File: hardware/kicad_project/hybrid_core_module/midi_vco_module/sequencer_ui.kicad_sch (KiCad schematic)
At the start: 53 parts, among them SW10 RotaryEncoder, SW6 SW_Push, SW7 SW_Push, SW8 SW_Push, SW9 SW_SP3T_NR01103, U25 MCP23017_SO

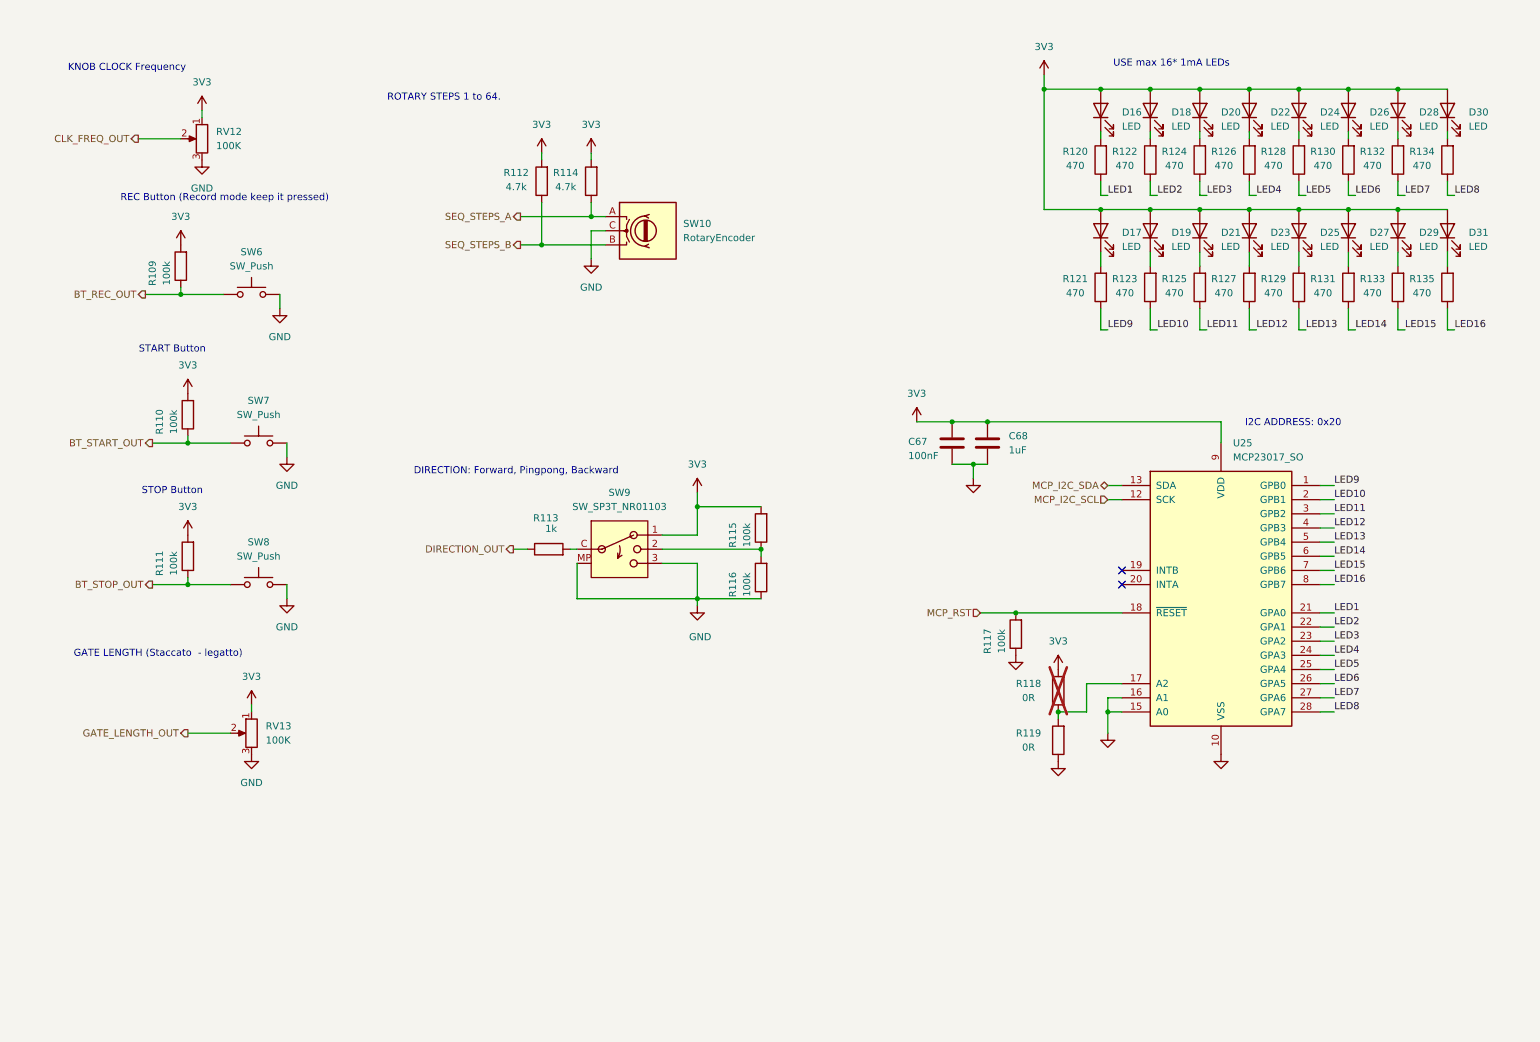
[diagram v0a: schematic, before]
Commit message: Schematic updated. Components Footprint assignment started. Waiting for components mechanical validation before starting layout.
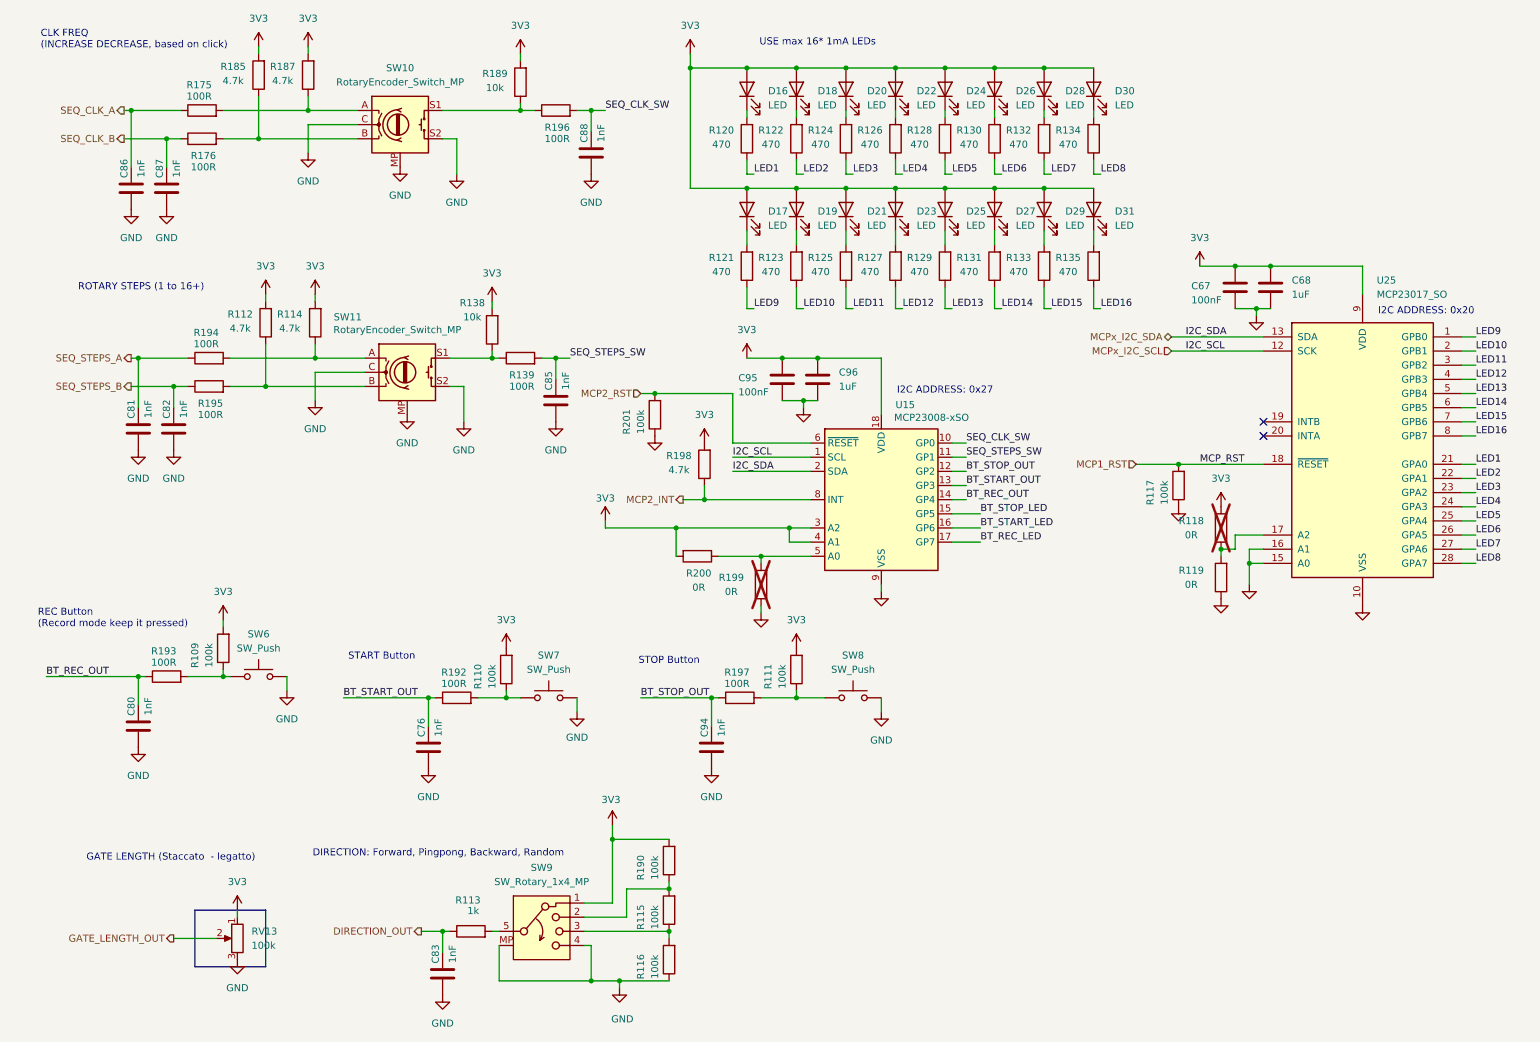
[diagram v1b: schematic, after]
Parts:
- removed RV12: 100K, symbol Device:R_Potentiometer
- removed SW10: RotaryEncoder, symbol Device:RotaryEncoder
- removed SW9: SW_SP3T_NR01103, Button_Switch_THT:SW_NKK_NR01, symbol Switch:SW_SP3T_NR01103
- added C76, C80, C81, C82, C83, C85, C86, C87, C88, C94: 1nF, Capacitor_SMD:C_0402_1005Metric, symbol Device:C
- added C95: 100nF, Capacitor_SMD:C_0402_1005Metric, symbol Device:C
- added C96: 1uF, Capacitor_SMD:C_0805_2012Metric, symbol Device:C
- added R138, R189: 10k, Resistor_SMD:R_0402_1005Metric, symbol Device:R
- added R139, R175, R176, R192, R193, R194, R195, R196, R197: 100R, Resistor_SMD:R_0402_1005Metric, symbol Device:R
- added R185, R187, R198: 4.7k, Resistor_SMD:R_0402_1005Metric, symbol Device:R
- added R190, R201: 100k, Resistor_SMD:R_0402_1005Metric, symbol Device:R
- added R199, R200: 0R, Resistor_SMD:R_0402_1005Metric, symbol Device:R
- added SW10, SW11: RotaryEncoder_Switch_MP, symbol Device:RotaryEncoder_Switch_MP
- added SW9: SW_Rotary_1x4_MP, symbol Switch:SW_Rotary_1x4_MP
- added U15: MCP23008-xSO, Package_SO:SOIC-18W_7.5x11.6mm_P1.27mm, symbol Interface_Expansion:MCP23008-xSO
- C67: footprint (none) -> Capacitor_SMD:C_0402_1005Metric; Manufacturer (none) -> MURATA; Manufacturer PartNumer (none) -> GRM155R71E104KE14J
- C68: footprint (none) -> Capacitor_SMD:C_0805_2012Metric; Manufacturer (none) -> MURATA; Manufacturer PartNumer (none) -> GRM219R71E105MA88J
- D17, D18, D19, D20, D21, D22, D23, D24, D25, D26, D27, D28, D29, D30, D31: footprint (none) -> mylib:LED-3528
- R109, R110, R111, R115, R116, R117: footprint (none) -> Resistor_SMD:R_0402_1005Metric; Manufacturer (none) -> YAGEO; Manufacturer PartNumer (none) -> RT0402FRE07100KL
- R112, R114: footprint (none) -> Resistor_SMD:R_0402_1005Metric; Manufacturer (none) -> YAGEO; Manufacturer PartNumer (none) -> RT0402FRE074K7L
- R113: footprint (none) -> Resistor_SMD:R_0402_1005Metric; Manufacturer (none) -> YAGEO; Manufacturer PartNumer (none) -> RT0402FRE071KL
- R118, R119: footprint (none) -> Resistor_SMD:R_0402_1005Metric; Manufacturer (none) -> YAGEO; Manufacturer PartNumer (none) -> RC0402FR-070RL
- R120, R121, R122, R123, R124, R125, R126, R127, R128, R129, R130, R131, R132, R133, R134, R135: footprint (none) -> Resistor_SMD:R_0402_1005Metric; Manufacturer (none) -> YAGEO; Manufacturer PartNumer (none) -> RT0402FRE07470RL
- RV13: value 100K -> 100k
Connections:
- net 3V3: now also C95.1, C96.1, R138.2, R185.2, R187.2, R189.2, R190.2, R198.2, R200.2, SW9.1, U15.18 (VDD), U15.3 (A2), U15.4 (A1); no longer R115.2
- net BT_REC_OUT: now also C80.2, R193.1, U15.14 (GP4); no longer R109.1, SW6.1
- net BT_START_OUT: now also C76.2, R192.1, U15.13 (GP3); no longer R110.1, SW7.1
- net BT_STOP_OUT: now also C94.2, R197.1, U15.12 (GP2); no longer R111.1, SW8.1
- net DIRECTION_OUT: now also C83.2
- net GND: now also C76.1, C80.1, C81.1, C82.1, C83.1, C85.1, C86.1, C87.1, C88.1, C94.1, C95.2, C96.2, R199.1, R201.1, SW10.C, SW10.MP, SW10.S2, SW11.C, SW11.MP, SW11.S2, SW9.4, SW9.MP, U15.9 (VSS)
- net SEQ_STEPS_A: now also C81.2, R194.1; no longer R114.1
- net SEQ_STEPS_B: now also C82.2, R195.1; no longer R112.1
- net at R115.1, R116.2: now also SW9.3
- net at R113.2: now also SW9.5
- net MCP_I2C_SCL renamed MCPx_I2C_SCL
- net MCPx_I2C_SCL: now also U15.1 (SCL)
- net MCP_I2C_SDA renamed MCPx_I2C_SDA
- net MCPx_I2C_SDA: now also U15.2 (SDA)
- net MCP_RST renamed MCP1_RST
- new net: R176.2, R185.1, SW10.B
- new net: R138.1, R139.1, SW11.S1
- new net: R189.1, R196.1, SW10.S1
- new net: R112.1, R195.2, SW11.B
- new net: R111.1, R197.2, SW8.1
- new net: R109.1, R193.2, SW6.1
- new net: R110.1, R192.2, SW7.1
- new net: R175.2, R187.1, SW10.A
- new net: R115.2, R190.1, SW9.2
- new net: R199.2, R200.1, U15.5 (A0)
- new net: R114.1, R194.2, SW11.A
- new net BT_REC_LED: U15.17 (GP7)
- new net BT_START_LED: U15.16 (GP6)
- new net BT_STOP_LED: U15.15 (GP5)
- new net MCP2_INT: R198.1, U15.8 (INT)
- new net MCP2_RST: R201.2, U15.6 (~{RESET})
- new net SEQ_CLK_A: C86.2, R175.1
- new net SEQ_CLK_B: C87.2, R176.1
- new net SEQ_CLK_SW: C88.2, R196.2, U15.10 (GP0)
- new net SEQ_STEPS_SW: C85.2, R139.2, U15.11 (GP1)
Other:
- note added: "CLK FREQ (INCREASE DECREASE, based on click)"
- note added: "DIRECTION: Forward, Pingpong, Backward, Random"
- note added: "I2C ADDRESS: 0x27"
- note added: "ROTARY STEPS (1 to 16+)"
- note removed: "DIRECTION: Forward, Pingpong, Backward"
- note removed: "KNOB CLOCK Frequency"
- note removed: "ROTARY STEPS 1 to 64."
- moved on the sheet: C67, C68, D16, D17, D18, D19, D20, D21, D22, D23, D24, D25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

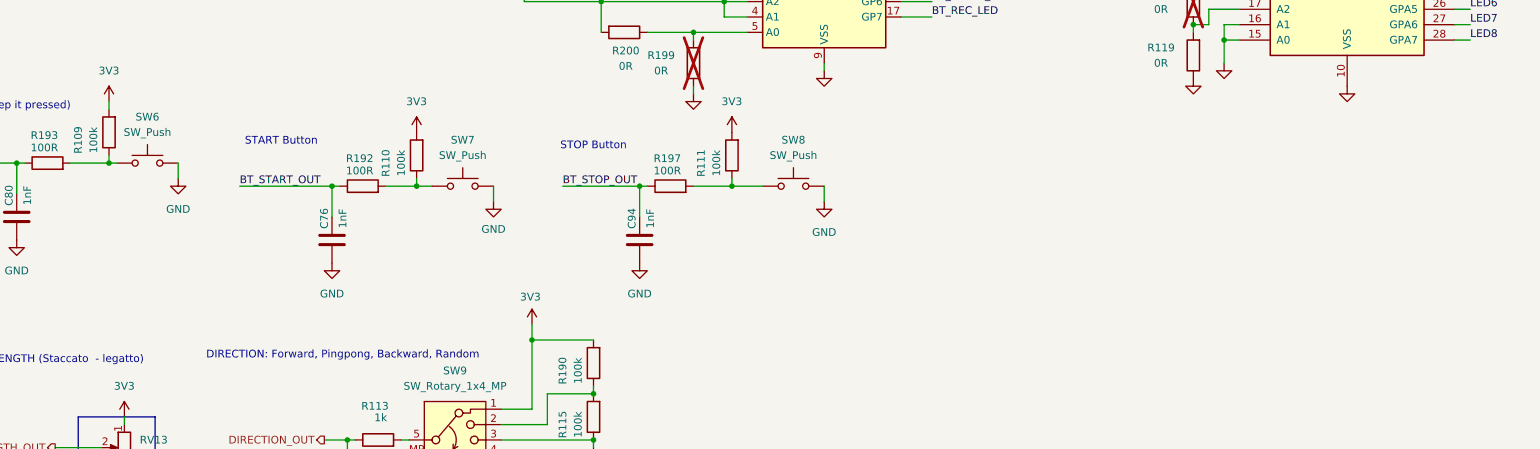
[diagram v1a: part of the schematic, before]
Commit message: - schematic updated  - PN and footprints added
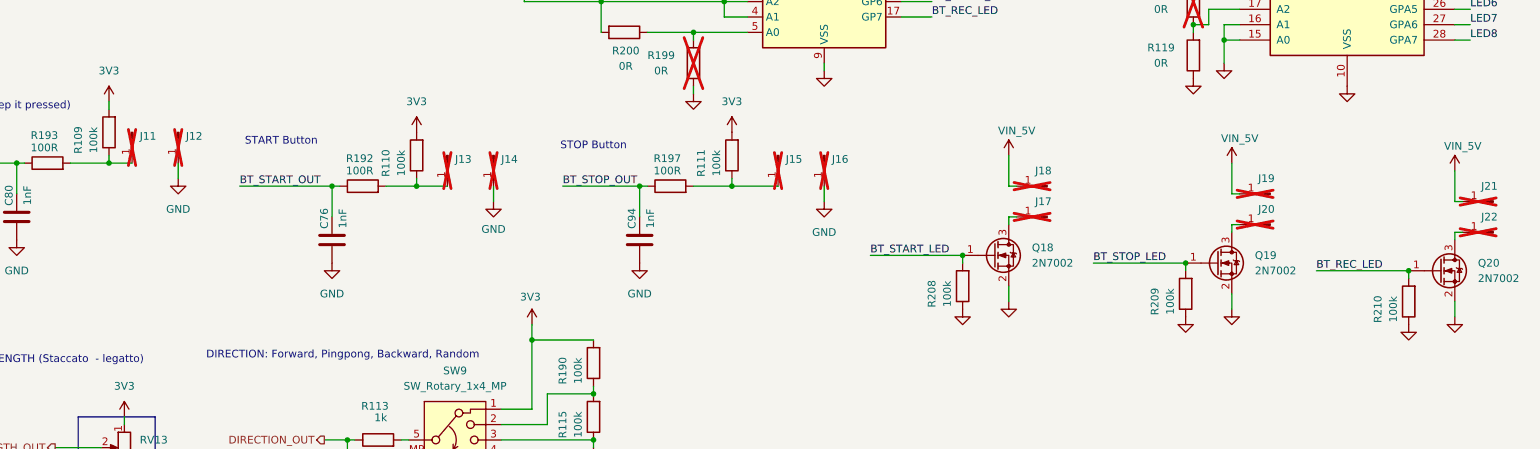
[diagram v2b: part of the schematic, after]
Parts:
- removed SW6, SW7, SW8: SW_Push, symbol Switch:SW_Push
- added J11, J12, J13, J14, J15, J16, J17, J18, J19, J20, J21, J22: Conn_01x01_Pin, Connector_PinHeader_1.00mm:PinHeader_1x01_P1.00mm_Vertical, symbol Connector:Conn_01x01_Pin
- added Q18, Q19, Q20: 2N7002, Package_TO_SOT_SMD:SOT-23, symbol Transistor_FET:2N7002
- added R208, R209, R210: 100k, Resistor_SMD:R_0402_1005Metric, symbol Device:R
- R138, R189: Manufacturer PartNumer RT0402FRE074K7L -> RT0402FRE0710KL
- RV13: footprint (none) -> Potentiometer_THT:Potentiometer_Bourns_3296W_Vertical; Manufacturer (none) -> KESHY; Manufacturer PartNumer (none) -> 3296W-104-LF
- SW10, SW11: footprint (none) -> Rotary_Encoder:RotaryEncoder_Alps_EC11E-Switch_Vertical_H20mm
- SW9: footprint (none) -> mylib:SR16 Rotary Band Switch; Manufacturer (none) -> ALIEXPRESS; Manufacturer PartNumer (none) -> SR16
- U15: Manufacturer (none) -> Microchip Technology; Manufacturer PartNumer (none) -> MCP23008T-E/SO
- U25: Manufacturer (none) -> Microchip Technology; Manufacturer PartNumer (none) -> MCP23017-E/SO
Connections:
- net BT_REC_LED: now also Q20.1 (G), R210.2
- net BT_START_LED: now also Q18.1 (G), R208.2
- net BT_STOP_LED: now also Q19.1 (G), R209.2
- net GND: now also J12.1 (Pin_1), J14.1 (Pin_1), J16.1 (Pin_1), Q18.2 (S), Q19.2 (S), Q20.2 (S), R208.1, R209.1, R210.1
- net at R111.1, R197.2: now also J15.1 (Pin_1)
- net at R109.1, R193.2: now also J11.1 (Pin_1)
- net at R110.1, R192.2: now also J13.1 (Pin_1)
- new net: J22.1 (Pin_1), Q20.3 (D)
- new net: J17.1 (Pin_1), Q18.3 (D)
- new net: J20.1 (Pin_1), Q19.3 (D)
- new net VIN_5V: J18.1 (Pin_1), J19.1 (Pin_1), J21.1 (Pin_1)
